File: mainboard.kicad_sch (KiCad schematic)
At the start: 34 parts, among them Q2 MMBT3906, Q3 SSM3J332R, Q4 MMBT3906, U3 NJM2845DL1, U4 MSP2807, U5 IM920c_ADP_IM920conn

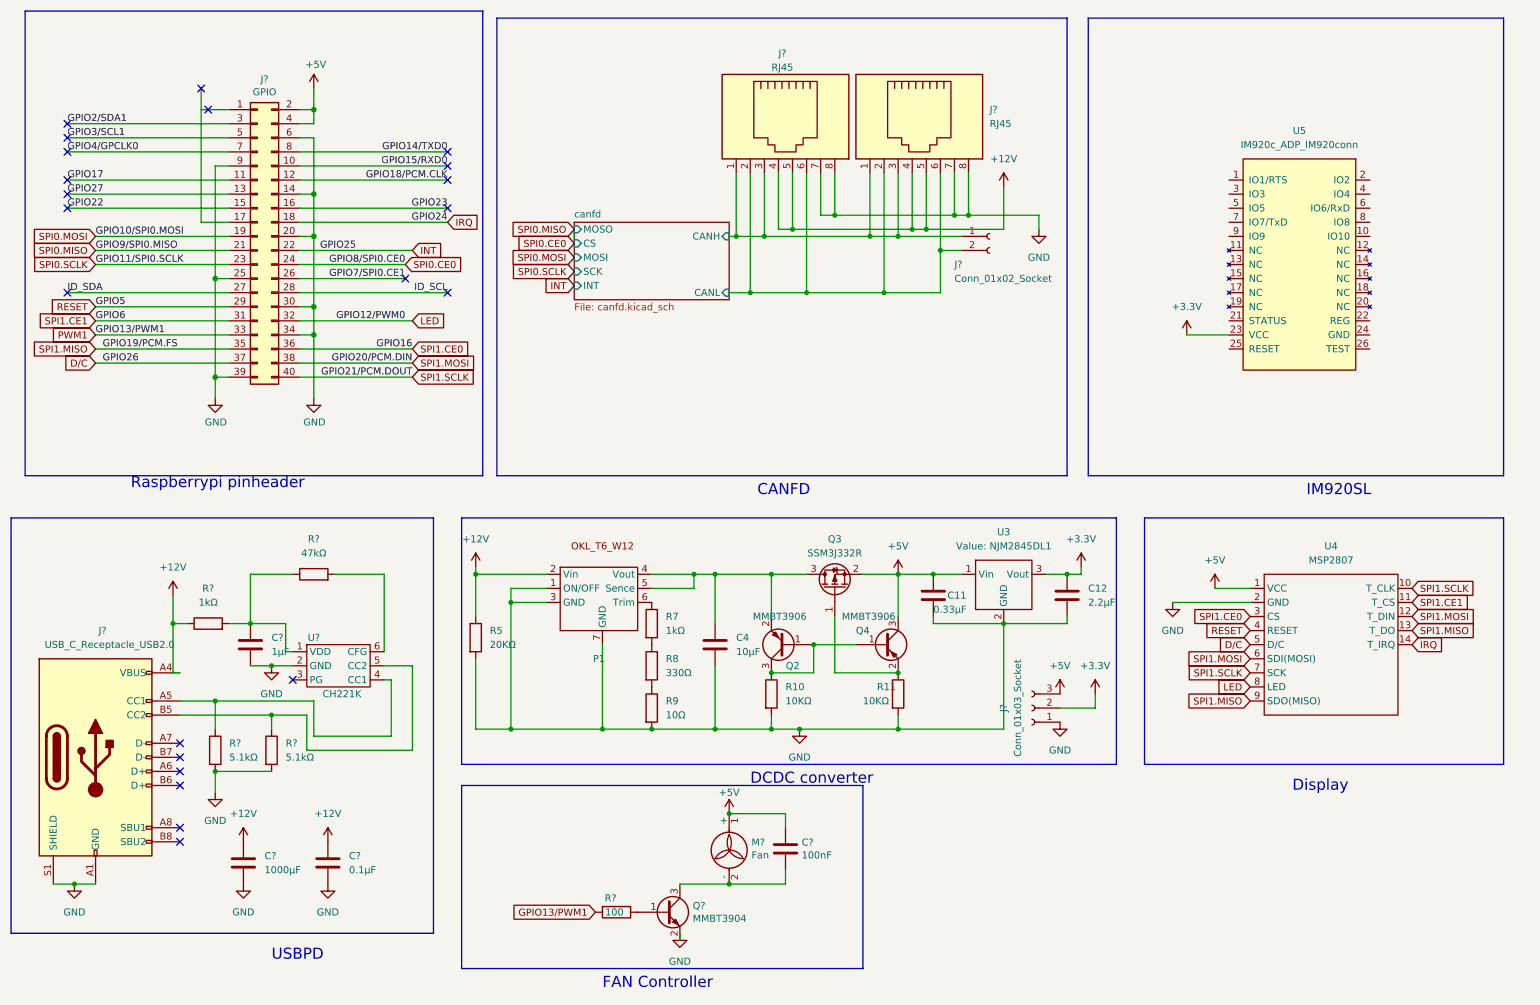
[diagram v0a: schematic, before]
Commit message: チップ抵抗に変更
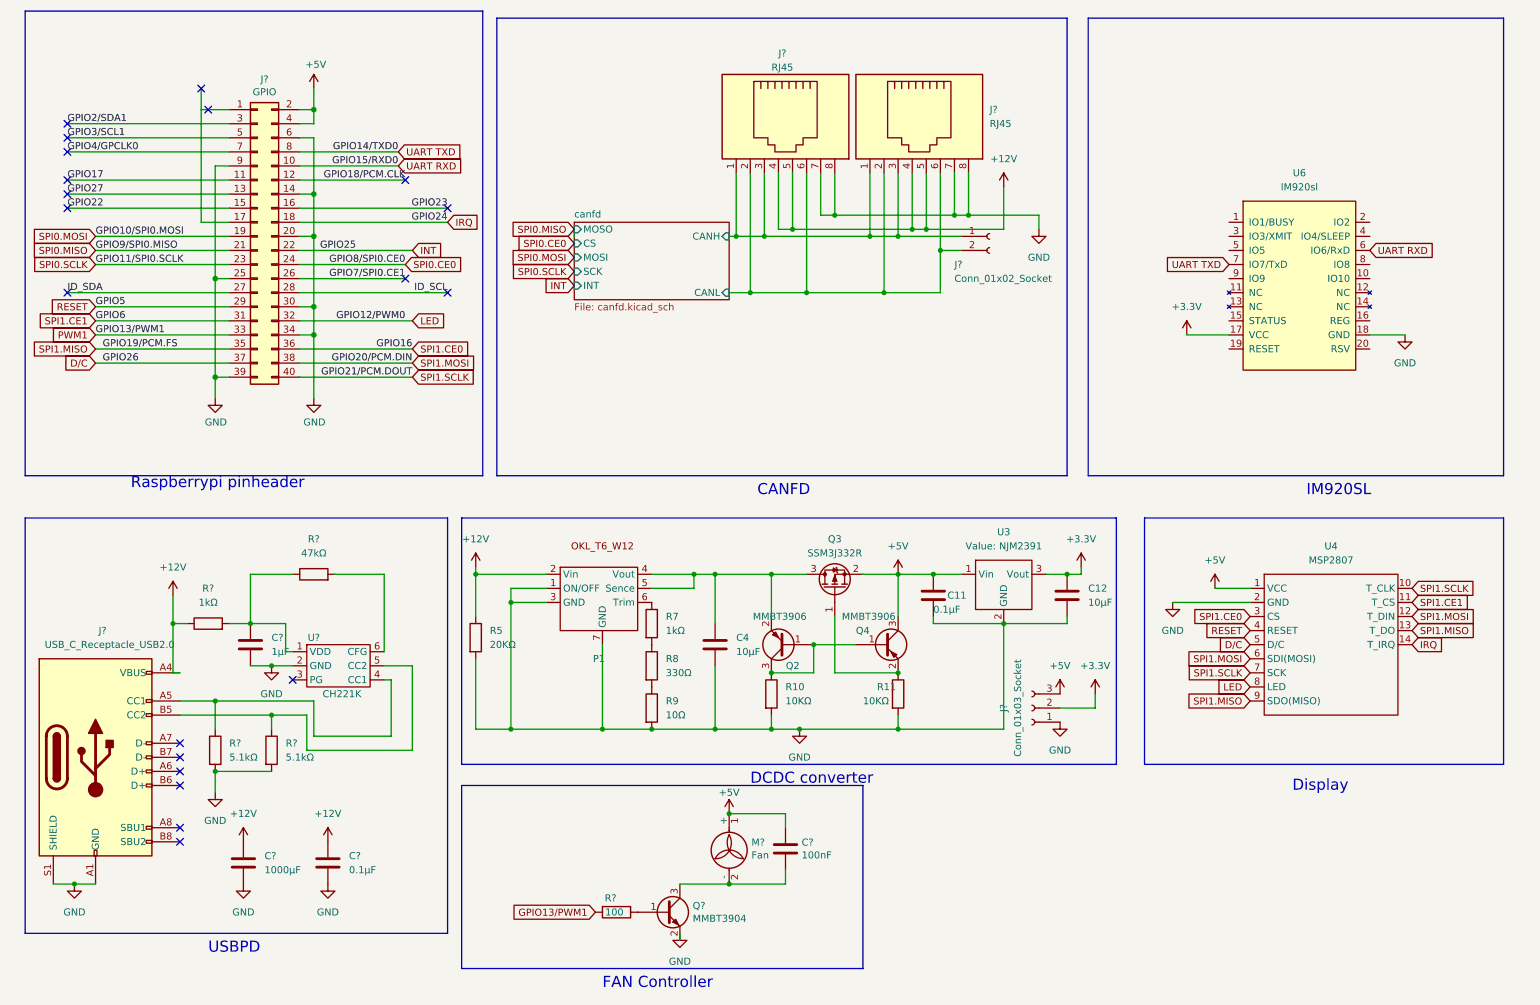
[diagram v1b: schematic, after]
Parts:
- removed U5: IM920c_ADP_IM920conn, interplan:IM920(IM920c_ADP), symbol interplan:IM920c_ADP_IM920conn
- added U6: IM920sl, interplan:IM920s, symbol interplan:IM920s
- C11: value 0.33μF -> 0.1μF; footprint Capacitor_THT:C_Disc_D4.7mm_W2.5mm_P5.00mm -> Capacitor_SMD:C_0603_1608Metric_Pad1.08x0.95mm_HandSolder
- C12: value 2.2µF -> 10µF; footprint Capacitor_THT:C_Disc_D4.7mm_W2.5mm_P5.00mm -> Capacitor_SMD:C_0805_2012Metric_Pad1.18x1.45mm_HandSolder
- C4, C?: footprint Capacitor_THT:C_Disc_D4.7mm_W2.5mm_P5.00mm -> Capacitor_SMD:C_0805_2012Metric_Pad1.18x1.45mm_HandSolder
- C?: footprint Capacitor_THT:C_Disc_D4.7mm_W2.5mm_P5.00mm -> Capacitor_SMD:C_0603_1608Metric_Pad1.08x0.95mm_HandSolder
- R10, R11, R9, R?: footprint Resistor_SMD:R_0201_0603Metric_Pad0.64x0.40mm_HandSolder -> Resistor_SMD:R_0805_2012Metric_Pad1.20x1.40mm_HandSolder
- R5, R8, R? (x3): footprint Resistor_THT:R_Axial_DIN0204_L3.6mm_D1.6mm_P5.08mm_Horizontal -> Resistor_SMD:R_0805_2012Metric_Pad1.20x1.40mm_HandSolder
- R7: footprint Resistor_SMD:R_0201_0603Metric -> Resistor_SMD:R_0805_2012Metric_Pad1.20x1.40mm_HandSolder
- R?: footprint Diode_SMD:D_0805_2012Metric -> Resistor_SMD:R_0805_2012Metric_Pad1.20x1.40mm_HandSolder
- U3: value NJM2845DL1 -> NJM2391; footprint Package_TO_SOT_SMD:TO-252-3_TabPin2 -> Package_TO_SOT_SMD:TO-252-2
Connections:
- net +3.3V: now also U6.17 (VCC)
- net GND: now also U6.18 (GND)
- net GPIO14/TXD0 renamed UART TXD
- net UART TXD: now also U6.7 (IO7/TxD)
- net GPIO15/RXD0 renamed UART RXD
- net UART RXD: now also U6.6 (IO6/RxD)
- no-connect marks 22 -> 20

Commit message: first commit
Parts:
- removed C11, C?: 0.1μF, Capacitor_SMD:C_0603_1608Metric_Pad1.08x0.95mm_HandSolder, symbol Device:C
- removed C12: 10µF, Capacitor_SMD:C_0805_2012Metric_Pad1.18x1.45mm_HandSolder, symbol Device:C
- removed C?: 1μF, Capacitor_SMD:C_0805_2012Metric_Pad1.18x1.45mm_HandSolder, symbol Device:C
- removed C?: 1000μF, Capacitor_THT:C_Radial_D10.0mm_H12.5mm_P5.00mm, symbol Device:C
- removed C?: 100nF, Capacitor_SMD:C_0805_2012Metric, symbol Device:C
- removed J?: Conn_01x03_Socket, Connector_PinHeader_2.54mm:PinHeader_1x03_P2.54mm_Vertical, symbol Connector:Conn_01x03_Socket
- removed J?: Conn_01x02_Socket, Connector_PinHeader_2.54mm:PinHeader_1x02_P2.54mm_Vertical, symbol Connector:Conn_01x02_Socket
- removed J?: USB_C_Receptacle_USB2.0, Connector_USB:USB_C_Receptacle_HCTL_HC-TYPE-C-16P-01A, symbol Connector:USB_C_Receptacle_USB2.0
- removed M?: Fan, pihat_cooling:fan_30mm, symbol Motor:Fan
- removed Q2, Q4: MMBT3906, Package_TO_SOT_SMD:SOT-23, symbol Transistor_BJT:MMBT3906
- removed Q3: SSM3J332R, Package_TO_SOT_SMD:SOT-23, symbol Device:Q_PMOS_GSD
- removed Q?: MMBT3904, Package_TO_SOT_SMD:SOT-23, symbol Transistor_BJT:MMBT3904
- removed R10, R11: 10KΩ, Resistor_SMD:R_0805_2012Metric_Pad1.20x1.40mm_HandSolder, symbol Device:R
- removed R5: 20KΩ, Resistor_SMD:R_0805_2012Metric_Pad1.20x1.40mm_HandSolder, symbol Device:R
- removed R? (x2): 5.1kΩ, Resistor_SMD:R_0805_2012Metric_Pad1.20x1.40mm_HandSolder, symbol Device:R
- removed R?: 100, Resistor_SMD:R_0805_2012Metric_Pad1.20x1.40mm_HandSolder, symbol Device:R
- removed R?: 47kΩ, Resistor_SMD:R_0805_2012Metric_Pad1.20x1.40mm_HandSolder, symbol Device:R
- removed R?: 1kΩ, Resistor_SMD:R_0805_2012Metric_Pad1.20x1.40mm_HandSolder, symbol Device:R
- removed U3: NJM2391, Package_TO_SOT_SMD:TO-252-2, symbol regulator:NJM2845DL1
- removed U4: MSP2807, MSP2807:MSP2807, symbol display:MSP2807
- removed U6: IM920sl, interplan:IM920s, symbol interplan:IM920s
- removed U?: CH221K, Package_TO_SOT_SMD:SOT-23-6, symbol CH:CH221K
- added C10: 10µF, Capacitor_SMD:C_0805_2012Metric_Pad1.18x1.45mm_HandSolder, symbol Device:C
- added C9: 0.1μF, Capacitor_SMD:C_0603_1608Metric_Pad1.08x0.95mm_HandSolder, symbol Device:C
- added C9: 22μF, Capacitor_SMD:C_0805_2012Metric_Pad1.18x1.45mm_HandSolder, symbol Device:C
- added IC1: AZ1117CH-3.3TRG1, OKL:SOT230P700X180-4N, symbol SamacSys_Parts:AZ1117CH-3.3TRG1
- added J11, J5, J6, J8: Conn_01x02, Connector_JST:JST_XH_B2B-XH-A_1x02_P2.50mm_Vertical, symbol Connector_Generic:Conn_01x02
- added J20: Conn_01x04_Socket, Connector_JST:JST_XH_B4B-XH-A_1x04_P2.50mm_Vertical, symbol Connector:Conn_01x04_Socket
- added J?: Conn_01x03_Socket, Connector_PinHeader_2.54mm:PinHeader_1x03_P2.54mm_Vertical, symbol Connector:Conn_01x03_Socket
- added Q5 (x2): IRFML8244TRPBF, Package_TO_SOT_SMD:SOT-23-3, symbol SamacSys_Parts:IRFML8244TRPBF
- added R39, R4, R40, R6, R7, R8: R, Resistor_SMD:R_0603_1608Metric_Pad0.98x0.95mm_HandSolder, symbol Device:R
- J? (x2): footprint akiRJ45:7810-8P8C -> OKL:7810-8P8C
- P1: value ~ -> OKLT6W12NC; footprint okL:OKLT6W12NC -> OKL:OKLT6W12NC
- renumbered C4 to C5, R8 to R2, R7 to R3, R9 to R5
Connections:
- net +12V: now also C9.1, J20.1 (Pin_1)
- net +3.3V: now also C10.1, IC1.2 (OUTPUT), IC1.4 (VOUT), J11.1 (Pin_1), J5.1 (Pin_1), J6.1 (Pin_1), J8.1 (Pin_1)
- net +5V: now also C5.1, P1.4 (Vout), P1.5 (Sence), C9.1, IC1.3 (INPUT)
- net GND: now also C10.2, C9.2, C9.2, IC1.1 (ADJ/GND), J?.1 (Pin_1), Q5.2 (S), Q5.2 (S), R39.1, R4.2, R40.1, R6.2, R7.2, R8.2
- net canfd/CANH: now also J?.3 (Pin_3)
- net canfd/CANL: now also J?.2 (Pin_2)
- net D/C renamed EN_3
- net GPIO13/PWM1 renamed EN_1
- net GPIO17 renamed LED_B
- net LED_B: now also Q5.1 (G), R40.2
- net GPIO27 renamed LED_R
- net LED_R: now also Q5.1 (G), R39.2
- net LED renamed limit1
- net limit1: now also J5.2 (Pin_2), R4.1
- net SPI1.CE0 renamed limit2
- net limit2: now also J6.2 (Pin_2), R6.1
- net SPI1.MISO renamed EN_2
- net SPI1.MOSI renamed limit3
- net limit3: now also J8.2 (Pin_2), R7.1
- net SPI1.SCLK renamed limit4
- net limit4: now also J11.2 (Pin_2), R8.1
- new net: J20.2 (Pin_2), Q5.3 (D)
- new net: J20.4 (Pin_4), Q5.3 (D)
- no-connect marks 20 -> 9
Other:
- added sheet I2C (i2c.kicad_sch)
- note added: "Raspberrypi PinHeader"
- note removed: "FAN Controller"
- note removed: "IM920SL"
- note removed: "Raspberrypi pinheader"
- note removed: "USBPD"
- moved on the sheet: J?, R2, R3, R5

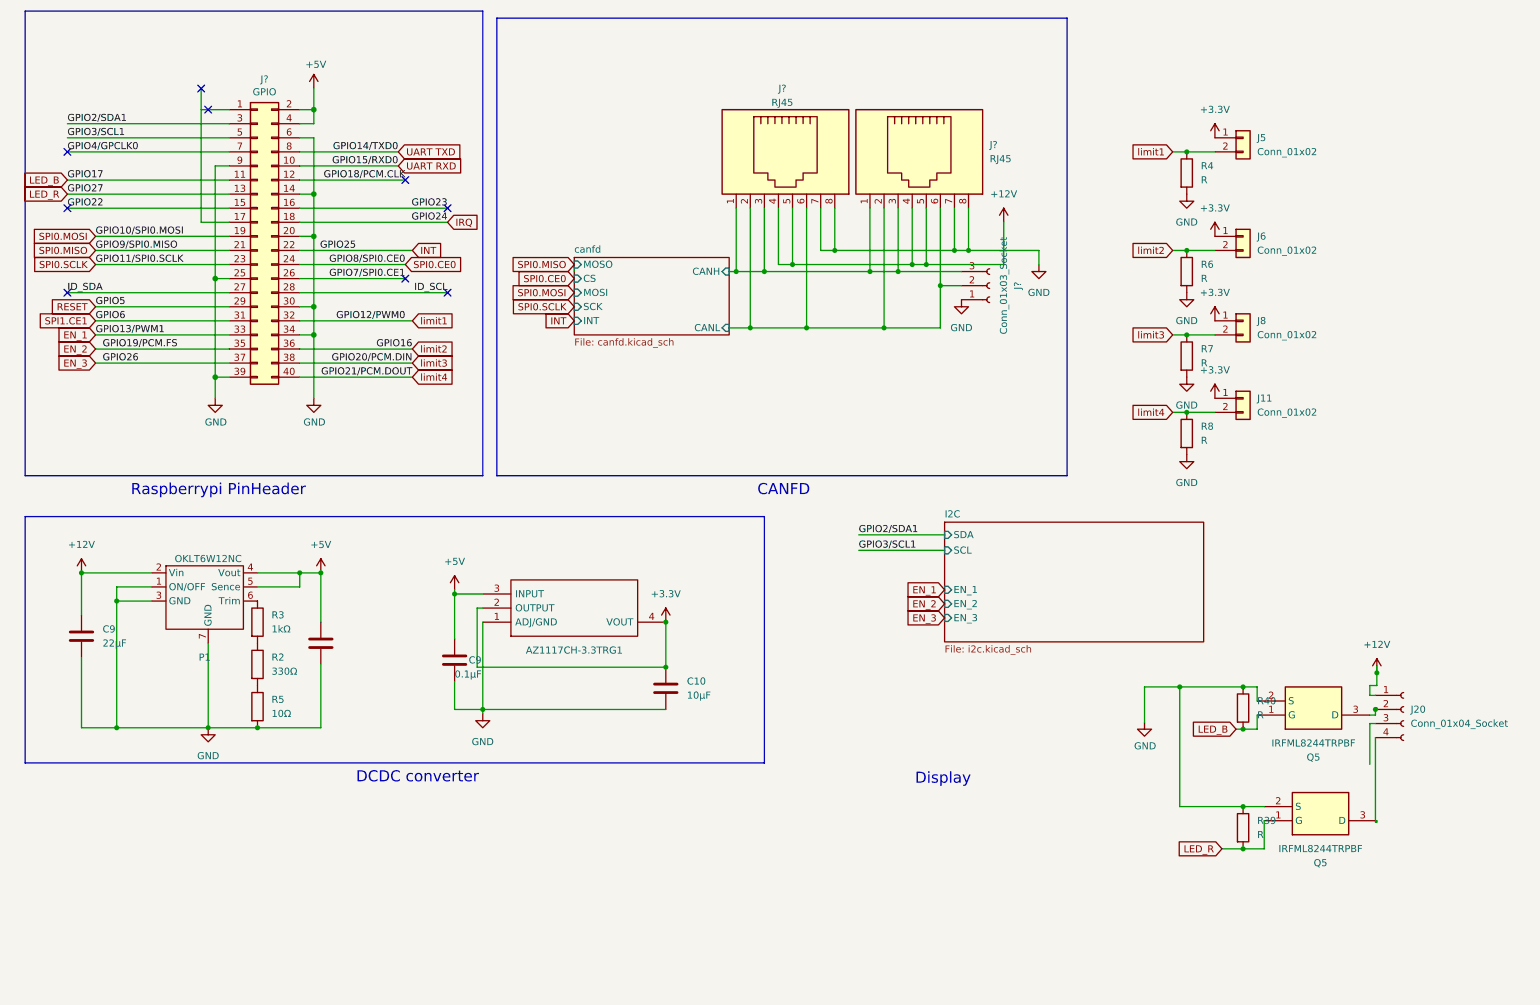
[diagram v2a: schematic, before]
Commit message: 2chに変更
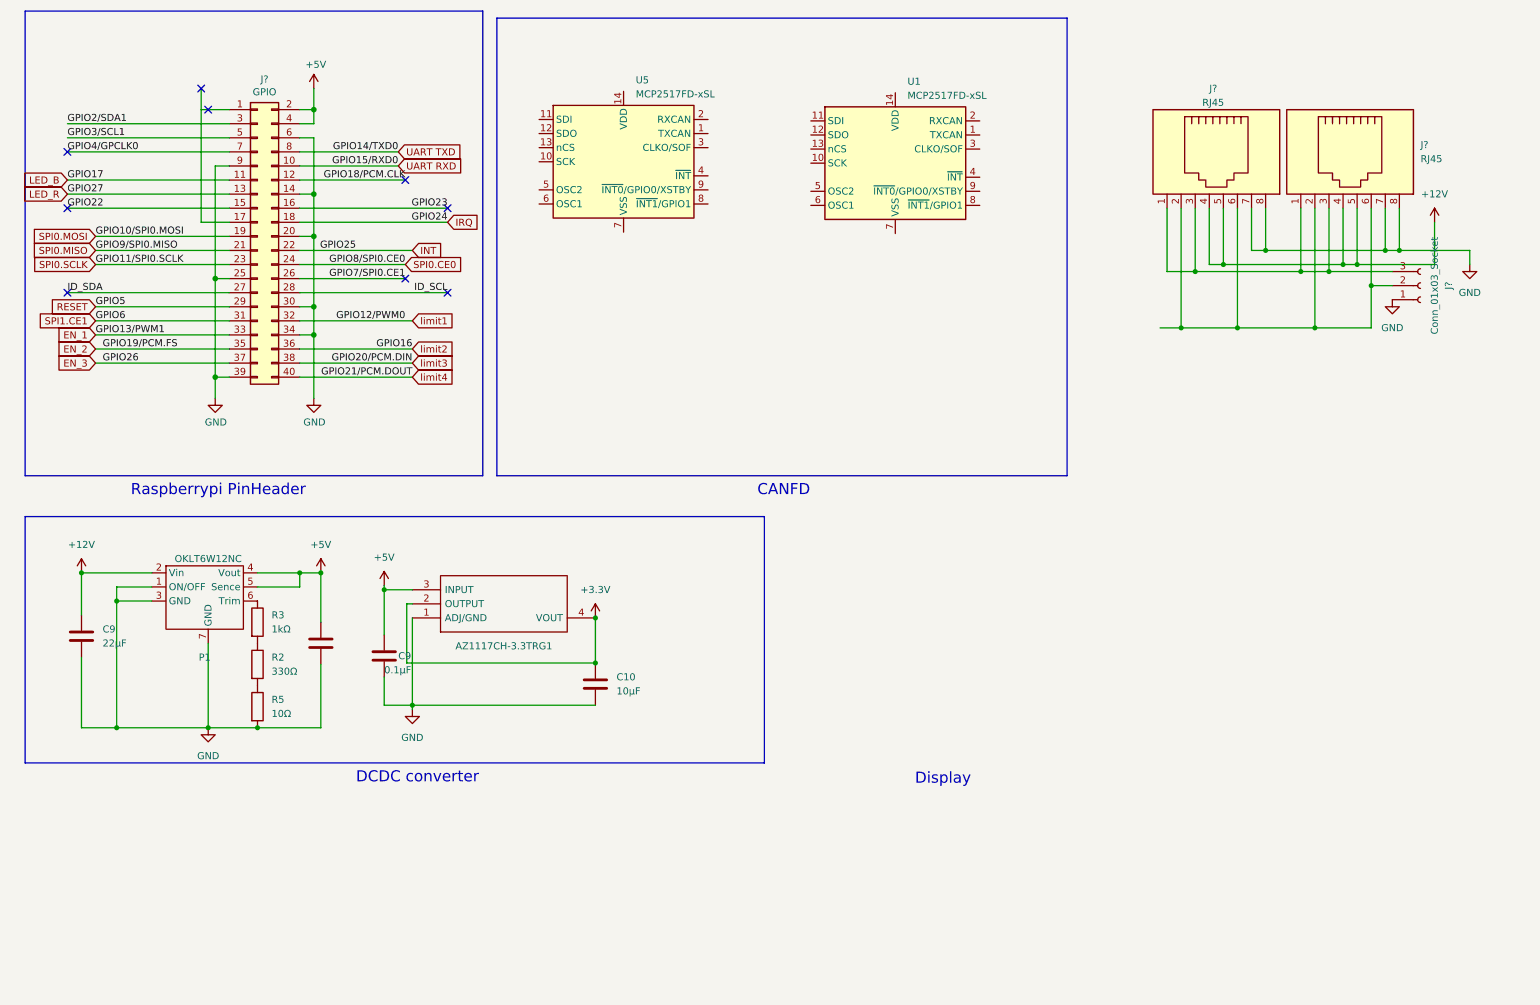
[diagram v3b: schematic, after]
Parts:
- removed J11, J5, J6, J8: Conn_01x02, Connector_JST:JST_XH_B2B-XH-A_1x02_P2.50mm_Vertical, symbol Connector_Generic:Conn_01x02
- removed J20: Conn_01x04_Socket, Connector_JST:JST_XH_B4B-XH-A_1x04_P2.50mm_Vertical, symbol Connector:Conn_01x04_Socket
- removed Q5 (x2): IRFML8244TRPBF, Package_TO_SOT_SMD:SOT-23-3, symbol SamacSys_Parts:IRFML8244TRPBF
- removed R39, R4, R40, R6, R7, R8: R, Resistor_SMD:R_0603_1608Metric_Pad0.98x0.95mm_HandSolder, symbol Device:R
- added U1, U5: MCP2517FD-xSL, Package_SO:SOIC-14_3.9x8.7mm_P1.27mm, symbol Interface_CAN_LIN:MCP2517FD-xSL
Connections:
- net canfd/CANH: no longer names the net of J?.1, J?.1, J?.3, J?.3, J?.3 (Pin_3)
- net canfd/CANL: no longer names the net of J?.2, J?.2, J?.2 (Pin_2), J?.6, J?.6
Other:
- removed sheet I2C
- removed sheet canfd
- moved on the sheet: C10, C9, J?
